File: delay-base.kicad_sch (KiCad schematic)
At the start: 24 parts, among them U1401 PT2399

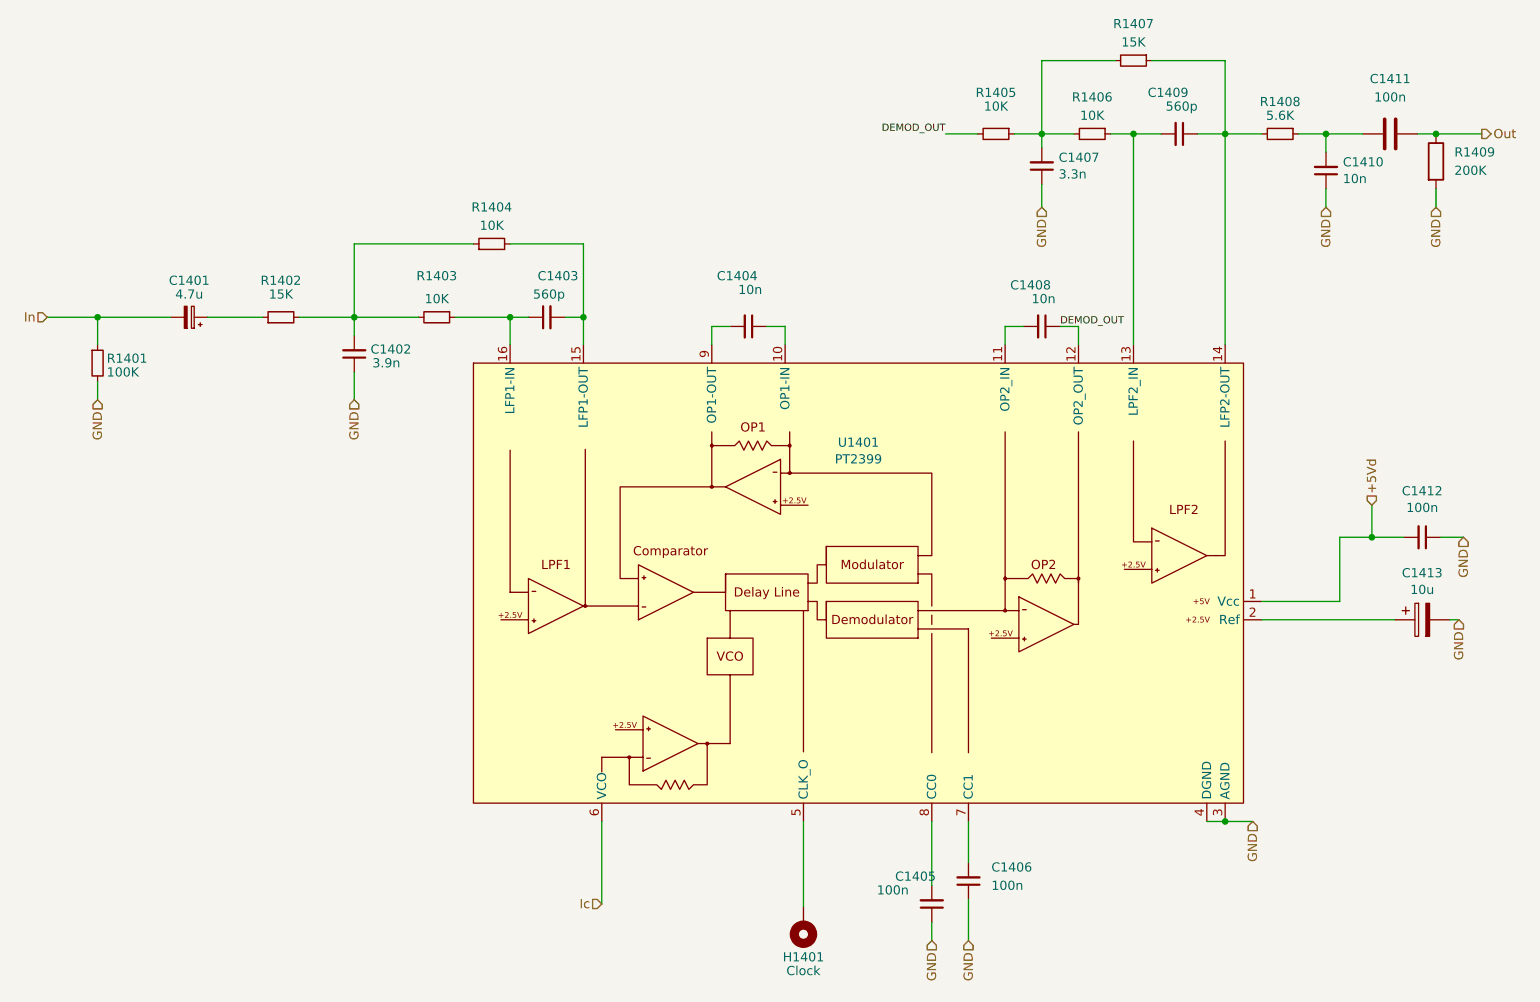
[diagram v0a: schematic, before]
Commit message: Delay layout done
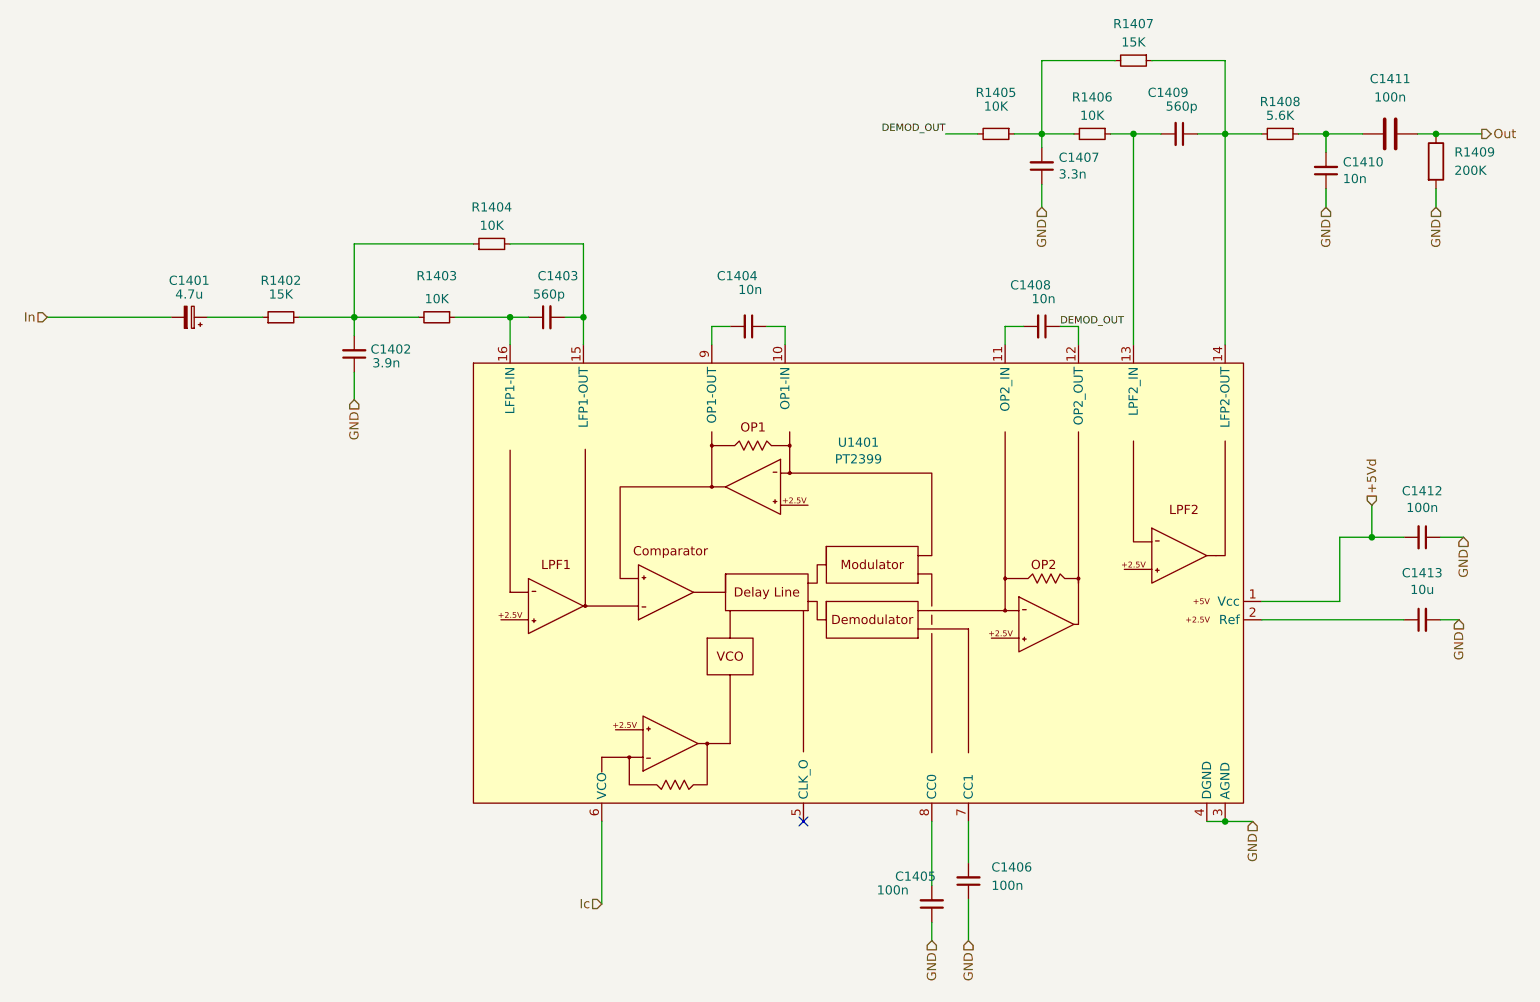
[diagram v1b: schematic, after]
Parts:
- removed H1401: Clock, TestPoint:TestPoint_Pad_4.0x4.0mm, symbol Mechanical:MountingHole_Pad
- removed R1401: 100K, Resistor_SMD:R_0603_1608Metric_Pad0.98x0.95mm_HandSolder, symbol Device:R_Small
- C1413: footprint Capacitor_SMD:C_Elec_4x5.4 -> Capacitor_SMD:C_0603_1608Metric_Pad1.08x0.95mm_HandSolder; symbol Device:C_Polarized -> Device:C_Small
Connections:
- no-connect marks 0 -> 1
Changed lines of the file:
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@@
   (junction (at 215.9 38.735) (diameter 0) (color 0 0 0 0)
   )
-  (junction (at 45.72 64.135) (diameter 0) (color 0 0 0 0)
-  )
   (junction (at 201.93 38.735) (diameter 0) (color 0 0 0 0)
   )
@@
   (junction (at 102.87 64.135) (diameter 0) (color 0 0 0 0)
   )
+  (no_connect (at 143.51 133.985))
   (wire (pts (xy 222.25 90.17) (xy 222.25 94.615))
     (stroke (width 0) (type default) (color 0 0 0 0))
@@
     (stroke (width 0) (type default) (color 0 0 0 0))
   )
-  (wire (pts (xy 234.315 106.045) (xy 233.045 106.045))
+  (wire (pts (xy 231.775 106.045) (xy 234.315 106.045))
     (stroke (width 0) (type default) (color 0 0 0 0))
   )
@@
     (stroke (width 0) (type default) (color 0 0 0 0))
   )
-  (wire (pts (xy 38.735 64.135) (xy 45.72 64.135))
-    (stroke (width 0) (type default) (color 0 0 0 0))
-  )
-  (wire (pts (xy 45.72 73.025) (xy 45.72 75.565))
-    (stroke (width 0) (type default) (color 0 0 0 0))
-  )
   (wire (pts (xy 222.25 94.615) (xy 226.695 94.615))
     (stroke (width 0) (type default) (color 0 0 0 0))
@@
     (stroke (width 0) (type default) (color 0 0 0 0))
   )
-  (wire (pts (xy 207.01 106.045) (xy 225.425 106.045))
+  (wire (pts (xy 207.01 106.045) (xy 226.695 106.045))
     (stroke (width 0) (type default) (color 0 0 0 0))
   )
@@
     (stroke (width 0) (type default) (color 0 0 0 0))
   )
-  (wire (pts (xy 143.51 133.985) (xy 143.51 145.796))
-    (stroke (width 0) (type default) (color 0 0 0 0))
-  )
   (wire (pts (xy 207.01 103.505) (xy 217.805 103.505))
     (stroke (width 0) (type default) (color 0 0 0 0))
@@
     (stroke (width 0) (type default) (color 0 0 0 0))
   )
-  (wire (pts (xy 45.72 64.135) (xy 45.72 67.945))
-    (stroke (width 0) (type default) (color 0 0 0 0))
-  )
   (wire (pts (xy 215.9 46.355) (xy 215.9 48.895))
     (stroke (width 0) (type default) (color 0 0 0 0))
@@
     (stroke (width 0) (type default) (color 0 0 0 0))
   )
-  (wire (pts (xy 45.72 64.135) (xy 55.88 64.135))
+  (wire (pts (xy 38.735 64.135) (xy 55.88 64.135))
     (stroke (width 0) (type default) (color 0 0 0 0))
   )
@@
   )
   (hierarchical_label "GND" (shape input) (at 234.315 106.045 270)
-    (effects (font (size 1.27 1.27)) (justify right))
-  )
-  (hierarchical_label "GND" (shape input) (at 45.72 75.565 270)
     (effects (font (size 1.27 1.27)) (justify right))
   )
@@
     (pin "2")
   )
-  (symbol (lib_id "Mechanical:MountingHole_Pad") (at 143.51 148.336 180) (unit 1)
-    (in_bom yes) (on_board yes)
-    (property "Reference" "H1401" (id 0) (at 143.51 152.781 0))
-    (property "Value" "Clock" (id 1) (at 143.51 154.686 0))
-    (property "Footprint" "TestPoint:TestPoint_Pad_4.0x4.0mm" (id 2) (at 143.51 148.336 0)
-      (effects (font (size 1.27 1.27)) hide)
-    )
-    (property "Datasheet" "~" (id 3) (at 143.51 148.336 0)
-      (effects (font (size 1.27 1.27)) hide)
-    )
-    (pin "1")
-  )
   (symbol (lib_id "Device:R_Small") (at 209.55 38.735 270) (unit 1)
     (in_bom yes) (on_board yes)
@@
     (pin "2")
   )
-  (symbol (lib_id "Device:C_Polarized") (at 229.235 106.045 90) (mirror x) (unit 1)
+  (symbol (lib_id "Device:C_Small") (at 229.235 106.045 90) (mirror x) (unit 1)
     (in_bom yes) (on_board yes)
     (property "Reference" "C1413" (id 0) (at 229.235 99.568 90))
     (property "Value" "10u" (id 1) (at 229.235 101.8794 90))
-    (property "Footprint" "Capacitor_SMD:C_Elec_4x5.4" (id 2) (at 233.045 107.0102 0)
+    (property "Footprint" "Capacitor_SMD:C_0603_1608Metric_Pad1.08x0.95mm_HandSolder" (id 2) (at 229.235 106.045 0)
       (effects (font (size 1.27 1.27)) hide)
     )
@@
       (effects (font (size 1.27 1.27)) hide)
     )
-    (pin "1")
-    (pin "2")
-  )
-  (symbol (lib_id "Device:R_Small") (at 45.72 70.485 0) (unit 1)
-    (in_bom yes) (on_board yes)
-    (property "Reference" "R1401" (id 0) (at 46.99 69.85 0)
-      (effects (font (size 1.27 1.27)) (justify left))
-    )
-    (property "Value" "100K" (id 1) (at 46.99 71.755 0)
-      (effects (font (size 1.27 1.27)) (justify left))
-    )
-    (property "Footprint" "Resistor_SMD:R_0603_1608Metric_Pad0.98x0.95mm_HandSolder" (id 2) (at 45.72 70.485 0)
-      (effects (font (size 1.27 1.27)) hide)
-    )
-    (property "Datasheet" "~" (id 3) (at 45.72 70.485 0)
-      (effects (font (size 1.27 1.27)) hide)
-    )

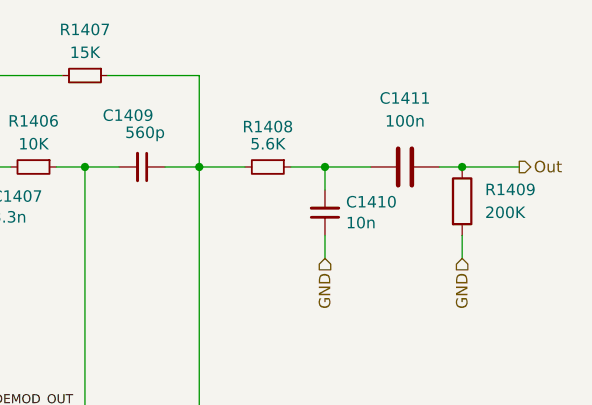
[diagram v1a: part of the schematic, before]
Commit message: Increase the size of dc blocking caps
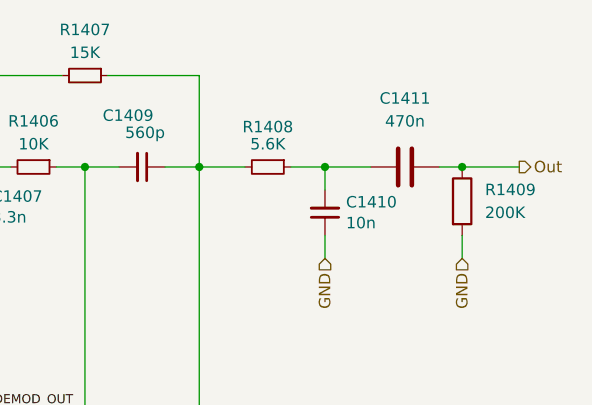
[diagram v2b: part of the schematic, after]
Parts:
- C1411: value 100n -> 470n; footprint Capacitor_SMD:C_0603_1608Metric_Pad1.08x0.95mm_HandSolder -> Capacitor_SMD:C_0805_2012Metric_Pad1.18x1.45mm_HandSolder
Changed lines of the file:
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@@
     (in_bom yes) (on_board yes) (fields_autoplaced)
     (property "Reference" "C1411" (id 0) (at 224.79 31.115 90))
-    (property "Value" "100n" (id 1) (at 224.79 33.655 90))
-    (property "Footprint" "Capacitor_SMD:C_0603_1608Metric_Pad1.08x0.95mm_HandSolder" (id 2) (at 228.6 37.7698 0)
+    (property "Value" "470n" (id 1) (at 224.79 33.655 90))
+    (property "Footprint" "Capacitor_SMD:C_0805_2012Metric_Pad1.18x1.45mm_HandSolder" (id 2) (at 228.6 37.7698 0)
       (effects (font (size 1.27 1.27)) hide)
     )

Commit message: Add JLC parts numbers
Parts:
- C1401: LCSC (none) -> C781889; Role (none) -> audio-coupling
- C1402: LCSC C170145 -> C415537; Role (none) -> audio-filter
- C1403, C1409: LCSC C159763 -> C107054; Role (none) -> audio-filter
- C1404, C1408, C1410: LCSC C1710 -> C57112; Role (none) -> audio-filter
- C1405, C1406: LCSC C49678 -> C519438; Role (none) -> unknown
- C1407: LCSC C53175 -> C190576; Role (none) -> audio-filter
- C1411: LCSC (none) -> C651004; Role (none) -> audio-coupling
- C1412: LCSC (none) -> C497032; Role (none) -> ic-bypass
- C1413: LCSC (none) -> C380314; Role (none) -> psu-filter
- R1402, R1407: LCSC (none) -> C100780
- R1403, R1404, R1405, R1406: LCSC (none) -> C98220
- R1408: LCSC (none) -> C365194
- R1409: LCSC (none) -> C203392
- U1401: LCSC (none) -> C126407
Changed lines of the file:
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@@
       (effects (font (size 1.27 1.27)) hide)
     )
-    (property "LCSC" "C170145" (id 4) (at 81.28 69.215 0)
+    (property "LCSC" "C415537" (id 4) (at 81.28 69.215 0)
+      (effects (font (size 1.27 1.27)) hide)
+    )
+    (property "Role" "audio-filter" (id 5) (at 81.28 69.215 0)
       (effects (font (size 1.27 1.27)) hide)
     )
@@
       (effects (font (size 1.27 1.27)) hide)
     )
-    (property "LCSC" "C49678" (id 4) (at 161.29 145.415 0)
+    (property "LCSC" "C519438" (id 4) (at 161.29 145.415 0)
+      (effects (font (size 1.27 1.27)) hide)
+    )
+    (property "Role" "unknown" (id 5) (at 161.29 145.415 0)
       (effects (font (size 1.27 1.27)) hide)
     )
@@
       (effects (font (size 1.27 1.27)) hide)
     )
+    (property "LCSC" "C365194" (id 4) (at 209.55 38.735 0)
+      (effects (font (size 1.27 1.27)) hide)
+    )
     (pin "1")
     (pin "2")
@@
       (effects (font (size 1.27 1.27)) hide)
     )
-    (property "LCSC" "" (id 4) (at 229.235 106.045 0)
+    (property "LCSC" "C380314" (id 4) (at 229.235 106.045 0)
+      (effects (font (size 1.27 1.27)) hide)
+    )
+    (property "Role" "psu-filter" (id 5) (at 229.235 106.045 0)
       (effects (font (size 1.27 1.27)) hide)
     )
@@
       (effects (font (size 1.27 1.27)) hide)
     )
+    (property "LCSC" "C98220" (id 4) (at 100.33 53.975 0)
+      (effects (font (size 1.27 1.27)) hide)
+    )
     (pin "1")
     (pin "2")
@@
       (effects (font (size 1.27 1.27)) hide)
     )
-    (property "LCSC" "C159763" (id 4) (at 107.95 64.135 0)
+    (property "LCSC" "C107054" (id 4) (at 107.95 64.135 0)
+      (effects (font (size 1.27 1.27)) hide)
+    )
+    (property "Role" "audio-filter" (id 5) (at 107.95 64.135 0)
       (effects (font (size 1.27 1.27)) hide)
     )
@@
       (effects (font (size 1.27 1.27)) hide)
     )
+    (property "LCSC" "C98220" (id 4) (at 92.71 64.135 0)
+      (effects (font (size 1.27 1.27)) hide)
+    )
     (pin "1")
     (pin "2")
@@
       (effects (font (size 1.27 1.27)) hide)
     )
-    (property "LCSC" "C53175" (id 4) (at 176.53 43.18 0)
+    (property "LCSC" "C190576" (id 4) (at 176.53 43.18 0)
+      (effects (font (size 1.27 1.27)) hide)
+    )
+    (property "Role" "audio-filter" (id 5) (at 176.53 43.18 0)
       (effects (font (size 1.27 1.27)) hide)
     )
@@
       (effects (font (size 1.27 1.27)) hide)
     )
-    (property "LCSC" "C1710" (id 4) (at 176.53 65.405 0)
+    (property "LCSC" "C57112" (id 4) (at 176.53 65.405 0)
+      (effects (font (size 1.27 1.27)) hide)
+    )
+    (property "Role" "audio-filter" (id 5) (at 176.53 65.405 0)
       (effects (font (size 1.27 1.27)) hide)
     )
@@
       (effects (font (size 1.27 1.27)) hide)
     )
+    (property "LCSC" "C100780" (id 4) (at 71.12 64.135 0)
+      (effects (font (size 1.27 1.27)) hide)
+    )
     (pin "1")
     (pin "2")
@@
       (effects (font (size 1.27 1.27)) hide)
     )
+    (property "LCSC" "C100780" (id 4) (at 189.23 28.575 0)
+      (effects (font (size 1.27 1.27)) hide)
+    )
     (pin "1")
     (pin "2")
@@
       (effects (font (size 1.27 1.27)) hide)
     )
+    (property "LCSC" "C98220" (id 4) (at 170.18 38.735 0)
+      (effects (font (size 1.27 1.27)) hide)
+    )
     (pin "1")
     (pin "2")
@@
       (effects (font (size 1.27 1.27)) hide)
     )
-    (property "LCSC" "C1710" (id 4) (at 135.89 65.405 0)
+    (property "LCSC" "C57112" (id 4) (at 135.89 65.405 0)
+      (effects (font (size 1.27 1.27)) hide)
+    )
+    (property "Role" "audio-filter" (id 5) (at 135.89 65.405 0)
       (effects (font (size 1.27 1.27)) hide)
     )
@@
       (effects (font (size 1.27 1.27)) hide)
     )
-    (property "LCSC" "C49678" (id 4) (at 166.37 142.24 0)
+    (property "LCSC" "C519438" (id 4) (at 166.37 142.24 0)
+      (effects (font (size 1.27 1.27)) hide)
+    )
+    (property "Role" "unknown" (id 5) (at 166.37 142.24 0)
       (effects (font (size 1.27 1.27)) hide)
     )
@@
       (effects (font (size 1.27 1.27)) hide)
     )
-    (property "LCSC" "C1710" (id 4) (at 215.9 43.815 0)
+    (property "LCSC" "C57112" (id 4) (at 215.9 43.815 0)
+      (effects (font (size 1.27 1.27)) hide)
+    )
+    (property "Role" "audio-filter" (id 5) (at 215.9 43.815 0)
       (effects (font (size 1.27 1.27)) hide)
     )
@@
       (effects (font (size 1.27 1.27)) hide)
     )
+    (property "LCSC" "C98220" (id 4) (at 183.515 38.735 0)
+      (effects (font (size 1.27 1.27)) hide)
+    )
     (pin "1")
     (pin "2")
@@
       (effects (font (size 1.27 1.27)) hide)
     )
-    (property "LCSC" "" (id 4) (at 58.42 64.135 0)
+    (property "LCSC" "C781889" (id 4) (at 58.42 64.135 0)
+      (effects (font (size 1.27 1.27)) hide)
+    )
+    (property "Role" "audio-coupling" (id 5) (at 58.42 64.135 0)
       (effects (font (size 1.27 1.27)) hide)
     )
@@
       (effects (font (size 1.27 1.27)) hide)
     )
+    (property "LCSC" "C203392" (id 4) (at 231.14 42.545 0)
+      (effects (font (size 1.27 1.27)) hide)
+    )
     (pin "1")
     (pin "2")
@@
     )
     (property "Datasheet" "http://sound.westhost.com/pt2399.pdf" (id 3) (at 151.13 111.125 0)
+      (effects (font (size 1.27 1.27)) hide)
+    )
+    (property "LCSC" "C126407" (id 4) (at 151.13 100.965 0)
       (effects (font (size 1.27 1.27)) hide)
     )
@@
       (effects (font (size 1.27 1.27)) hide)
     )
-    (property "LCSC" "" (id 4) (at 229.235 94.615 0)
+    (property "LCSC" "C497032" (id 4) (at 229.235 94.615 0)
+      (effects (font (size 1.27 1.27)) hide)
+    )
+    (property "Role" "ic-bypass" (id 5) (at 229.235 94.615 0)
       (effects (font (size 1.27 1.27)) hide)
     )
@@
       (effects (font (size 1.27 1.27)) hide)
     )
-    (property "LCSC" "C159763" (id 4) (at 195.58 38.735 0)
+    (property "LCSC" "C107054" (id 4) (at 195.58 38.735 0)
+      (effects (font (size 1.27 1.27)) hide)
+    )
+    (property "Role" "audio-filter" (id 5) (at 195.58 38.735 0)
       (effects (font (size 1.27 1.27)) hide)
     )
@@
       (effects (font (size 1.27 1.27)) hide)
     )
+    (property "LCSC" "C651004" (id 4) (at 224.79 38.735 0)
+      (effects (font (size 1.27 1.27)) hide)
+    )
+    (property "Role" "audio-coupling" (id 5) (at 224.79 38.735 0)
+      (effects (font (size 1.27 1.27)) hide)
+    )
